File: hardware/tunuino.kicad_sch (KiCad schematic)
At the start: 2 parts, among them J102 AMPSEAL_35, J103 AMPSEAL_35

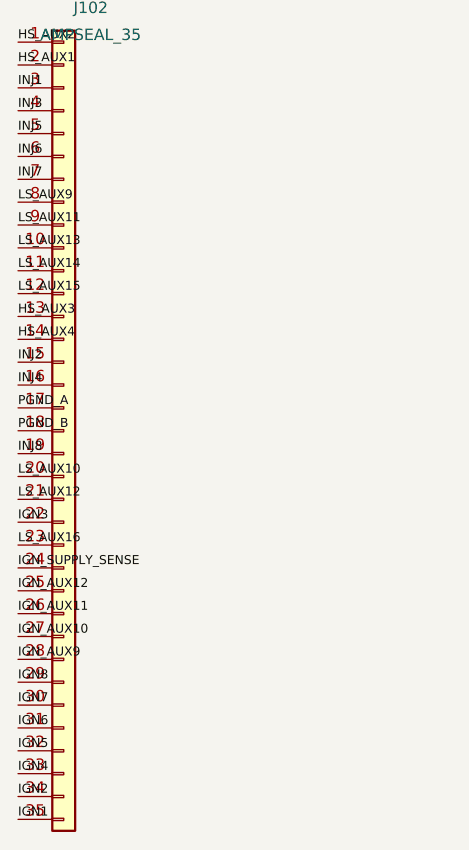
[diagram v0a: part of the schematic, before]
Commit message: Migrate Tunuino connector schematic to six cylinders and four-wire idle stepper
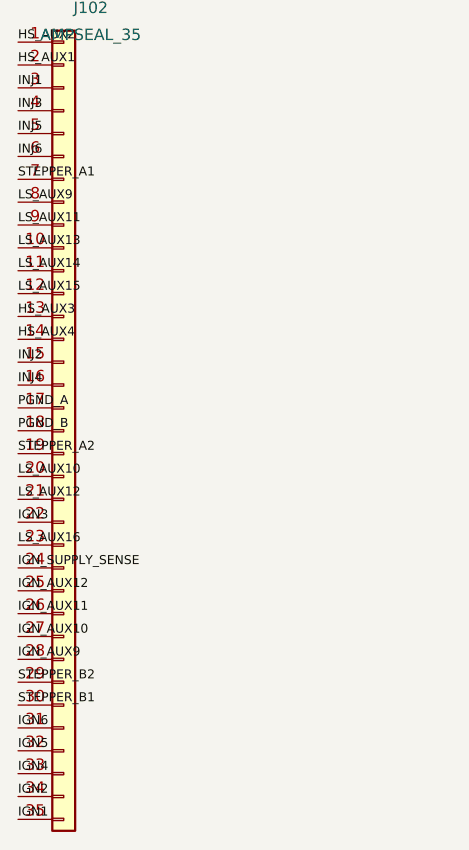
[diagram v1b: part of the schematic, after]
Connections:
- net IGN7 renamed STEPPER_B1
- net IGN8 renamed STEPPER_B2
- net INJ7 renamed STEPPER_A1
- net INJ8 renamed STEPPER_A2
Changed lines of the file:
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@@
   (label "PGND_A" (at 79.92 107.46 0) (effects (font (size 1.0 1.0)) (justify left bottom)))
   (label "PGND_B" (at 79.92 110 0) (effects (font (size 1.0 1.0)) (justify left bottom)))
-  (label "INJ8" (at 79.92 112.54 0) (effects (font (size 1.0 1.0)) (justify left bottom)))
+  (label "STEPPER_A2" (at 79.92 112.54 0) (effects (font (size 1.0 1.0)) (justify left bottom)))
   (label "HS_AUX1" (at 79.92 69.36 0) (effects (font (size 1.0 1.0)) (justify left bottom)))
   (label "LS_AUX10" (at 79.92 115.08 0) (effects (font (size 1.0 1.0)) (justify left bottom)))
@@
   (label "IGN_AUX10" (at 79.92 132.86 0) (effects (font (size 1.0 1.0)) (justify left bottom)))
   (label "IGN_AUX9" (at 79.92 135.4 0) (effects (font (size 1.0 1.0)) (justify left bottom)))
-  (label "IGN8" (at 79.92 137.94 0) (effects (font (size 1.0 1.0)) (justify left bottom)))
+  (label "STEPPER_B2" (at 79.92 137.94 0) (effects (font (size 1.0 1.0)) (justify left bottom)))
   (label "INJ1" (at 79.92 71.9 0) (effects (font (size 1.0 1.0)) (justify left bottom)))
-  (label "IGN7" (at 79.92 140.48 0) (effects (font (size 1.0 1.0)) (justify left bottom)))
+  (label "STEPPER_B1" (at 79.92 140.48 0) (effects (font (size 1.0 1.0)) (justify left bottom)))
   (label "IGN6" (at 79.92 143.02 0) (effects (font (size 1.0 1.0)) (justify left bottom)))
   (label "IGN5" (at 79.92 145.56 0) (effects (font (size 1.0 1.0)) (justify left bottom)))
@@
   (label "INJ5" (at 79.92 76.98 0) (effects (font (size 1.0 1.0)) (justify left bottom)))
   (label "INJ6" (at 79.92 79.52 0) (effects (font (size 1.0 1.0)) (justify left bottom)))
-  (label "INJ7" (at 79.92 82.06 0) (effects (font (size 1.0 1.0)) (justify left bottom)))
+  (label "STEPPER_A1" (at 79.92 82.06 0) (effects (font (size 1.0 1.0)) (justify left bottom)))
   (label "LS_AUX9" (at 79.92 84.6 0) (effects (font (size 1.0 1.0)) (justify left bottom)))
   (label "LS_AUX11" (at 79.92 87.14 0) (effects (font (size 1.0 1.0)) (justify left bottom)))
